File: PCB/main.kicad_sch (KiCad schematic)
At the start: 42 parts, among them J1 USB_C_Receptacle, J2 USB_C_Receptacle, J4 USB_C_Receptacle, J6 RJ45_Amphenol_RJMG1BD3B8K1ANR, M1 Fan_PC_Chassis, M2 Fan_PC_Chassis, M3 Fan_PC_Chassis, M4 Fan_PC_Chassis, SW1 SW_DPDT_x2, U2 LAN9512i, Y2 KC2520Z

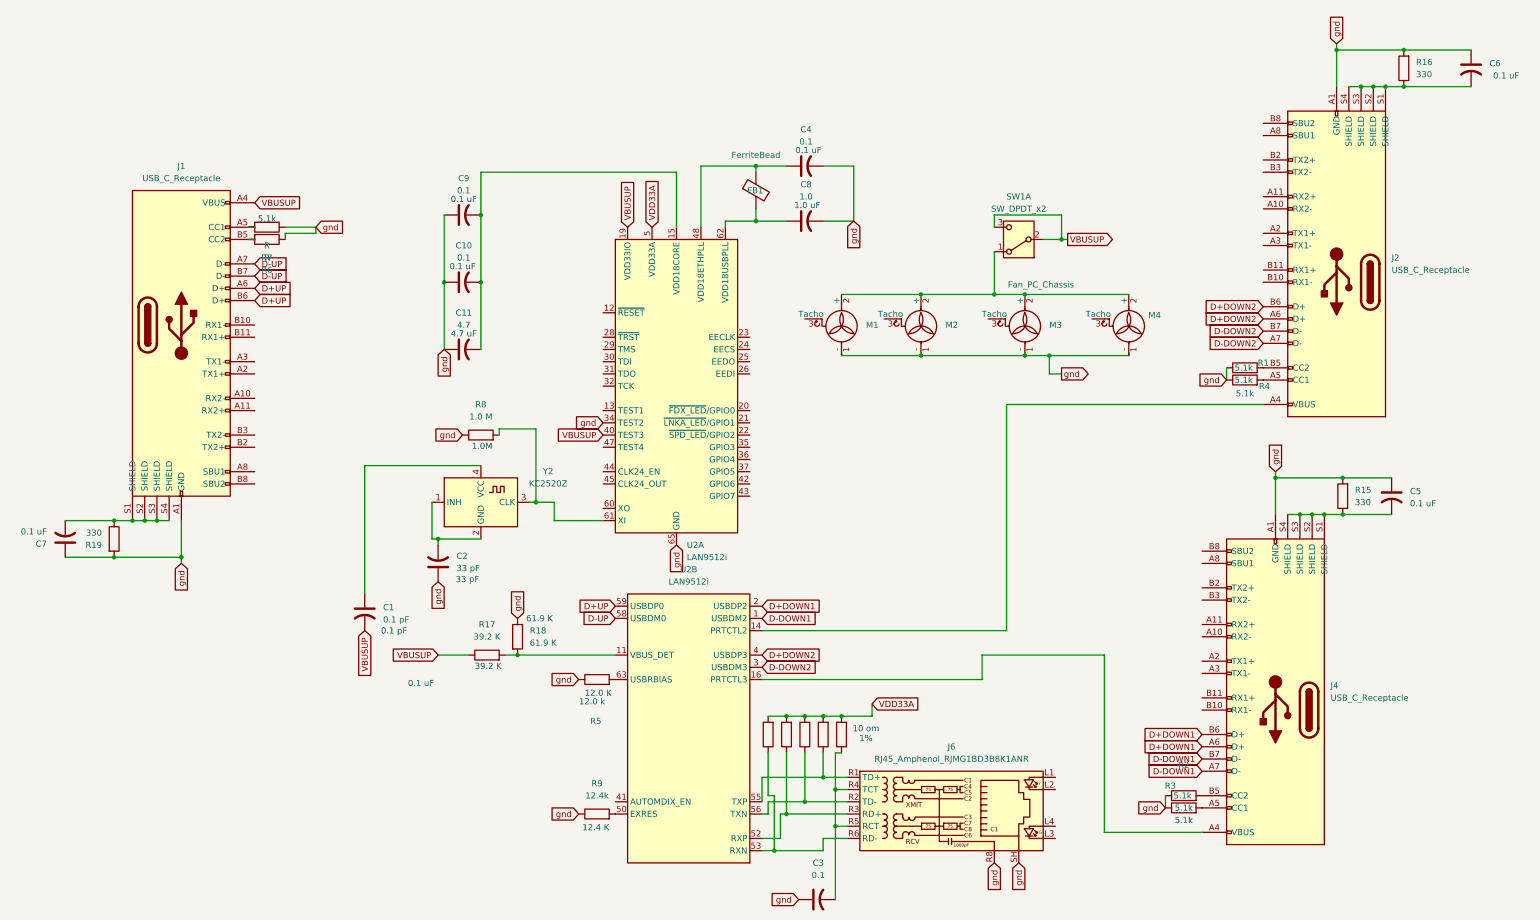
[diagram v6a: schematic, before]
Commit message: fixing footprints
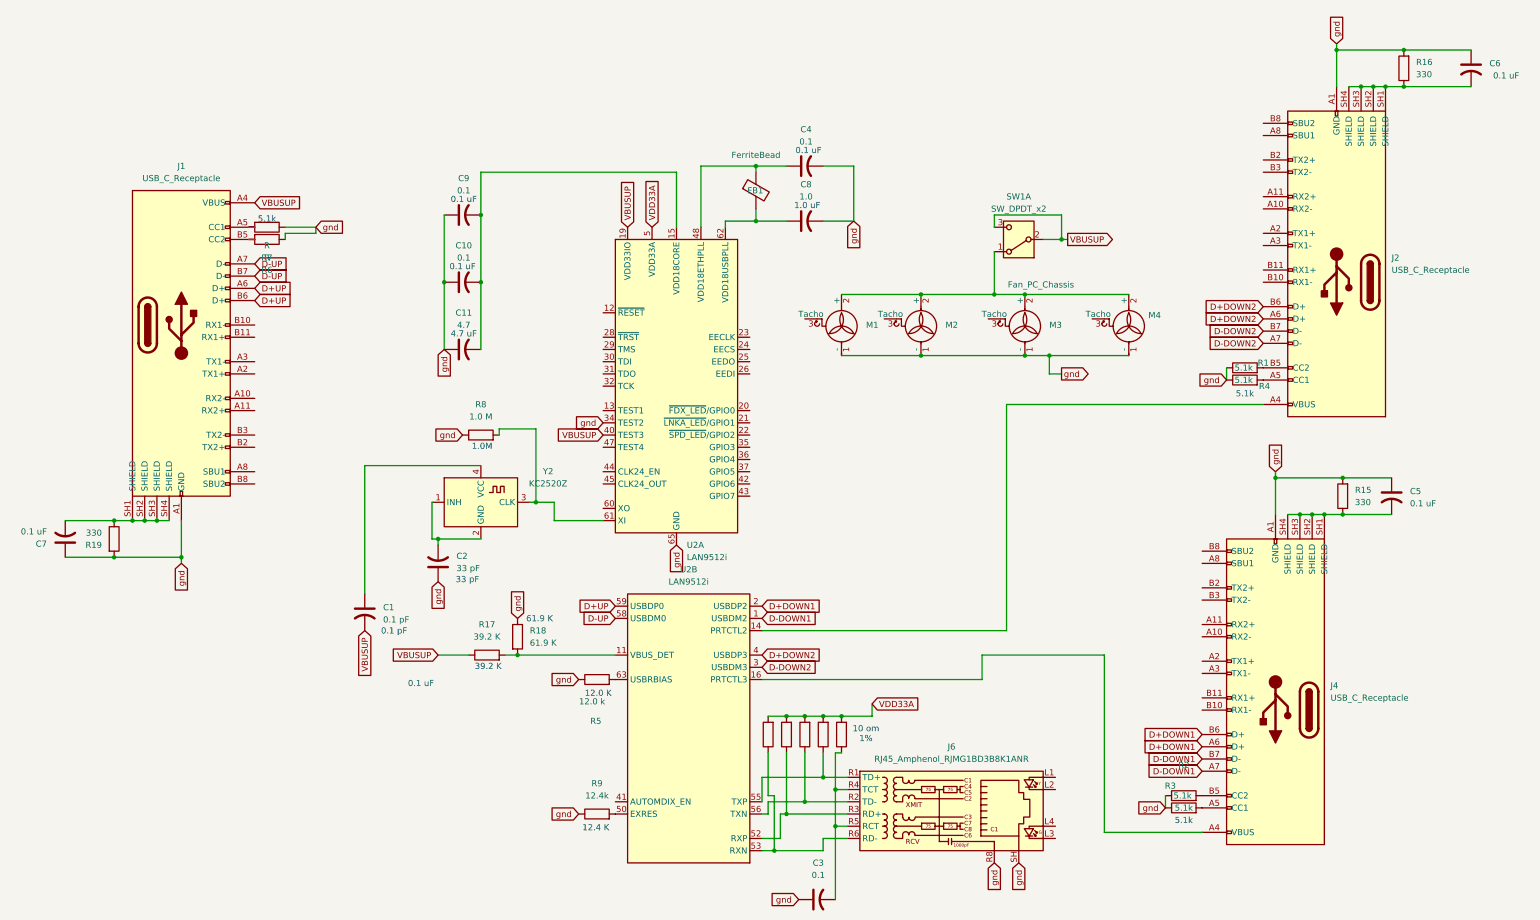
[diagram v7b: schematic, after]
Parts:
- J1, J2, J4: footprint footprintsweeeeee:12401826_AMP -> footprintsweeeeee:AMPHENOL_12401826E412A
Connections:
- new net: C7.2, J1.SH1 (SHIELD), J1.SH2 (SHIELD), J1.SH3 (SHIELD), J1.SH4 (SHIELD), R19.1
- new net: C6.2, J2.SH1 (SHIELD), J2.SH2 (SHIELD), J2.SH3 (SHIELD), J2.SH4 (SHIELD), R16.1
- new net: C5.2, J4.SH1 (SHIELD), J4.SH2 (SHIELD), J4.SH3 (SHIELD), J4.SH4 (SHIELD), R15.1
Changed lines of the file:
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@@
 	)
 	(symbol
+		(lib_name "USB_C_Receptacle_2")
 		(lib_id "MINE:USB_C_Receptacle")
 		(at 30.48 50.8 0)
@@
 			)
 		)
-		(property "Footprint" "footprintsweeeeee:12401826_AMP"
+		(property "Footprint" "footprintsweeeeee:AMPHENOL_12401826E412A"
 			(at 34.29 50.8 0)
 			(effects
@@
 		(pin "A1"
 		)
-		(pin "S3"
+		(pin "SH3"
 		)
 		(pin "B9"
@@
 		(pin "A7"
 		)
-		(pin "S2"
-		)
-		(pin "S1"
+		(pin "SH4"
+		)
+		(pin "SH1"
 		)
 		(pin "B1"
 		)
-		(pin "S4"
+		(pin "SH2"
 		)
 		(pin "A9"
@@
 	)
 	(symbol
+		(lib_name "USB_C_Receptacle_1")
 		(lib_id "MINE:USB_C_Receptacle")
 		(at 270.51 41.91 180)
@@
 			)
 		)
-		(property "Footprint" "footprintsweeeeee:12401826_AMP"
+		(property "Footprint" "footprintsweeeeee:AMPHENOL_12401826E412A"
 			(at 266.7 41.91 0)
 			(effects
@@
 			)
 		)
-		(pin "S2"
-		)
-		(pin "S4"
-		)
-		(pin "S1"
-		)
-		(pin "S3"
+		(pin "SH4"
+		)
+		(pin "SH2"
+		)
+		(pin "SH1"
+		)
+		(pin "SH3"
 		)
 		(pin "A4"
@@
 			)
 		)
-		(property "Footprint" "footprintsweeeeee:12401826_AMP"
+		(property "Footprint" "footprintsweeeeee:AMPHENOL_12401826E412A"
 			(at 254 130.81 0)
 			(effects
@@
 		(pin "A11"
 		)
-		(pin "S4"
+		(pin "SH4"
 		)
 		(pin "B1"
@@
 		(pin "B8"
 		)
-		(pin "S3"
-		)
-		(pin "S2"
+		(pin "SH1"
+		)
+		(pin "SH2"
 		)
 		(pin "B12"
 		)
-		(pin "S1"
+		(pin "SH3"
 		)
 		(pin "B5"
